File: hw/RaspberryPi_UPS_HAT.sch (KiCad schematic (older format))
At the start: 57 parts, among them J1 ISP, J2 Raspberry_Pi_2_3, J3 BAT, J4 COM, J5 FAN, J6 USB4125-GF-A_REVA, Q1 BC846, Q2 BC846, Q3 AO3401A, Q4 AO3401A, Q5 AO3401A, SW1 BTN, SW2 RST, U1 MIC5219-3.3YM5, U2 ATtiny841-SSU, U3 DS18B20, U4 MT3608, U5 LTC4054ES5-4.2

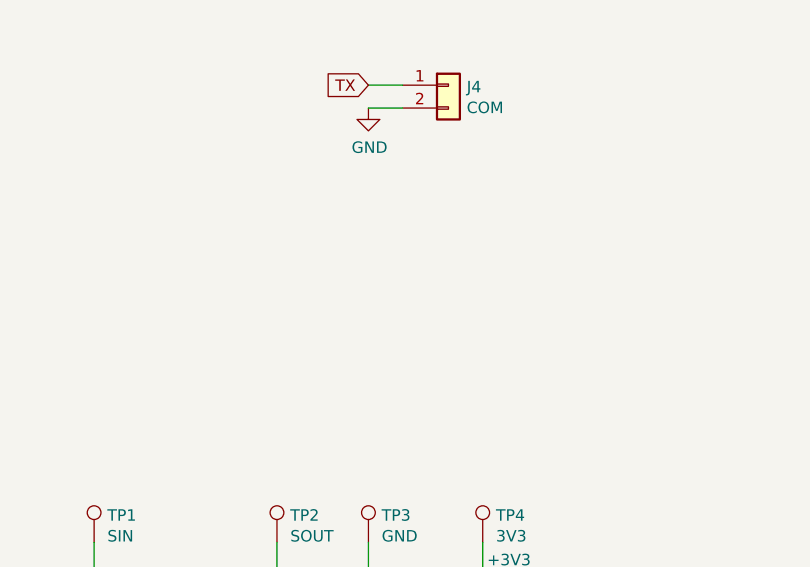
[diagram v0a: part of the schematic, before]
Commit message: update: make BTN available as optional pin header
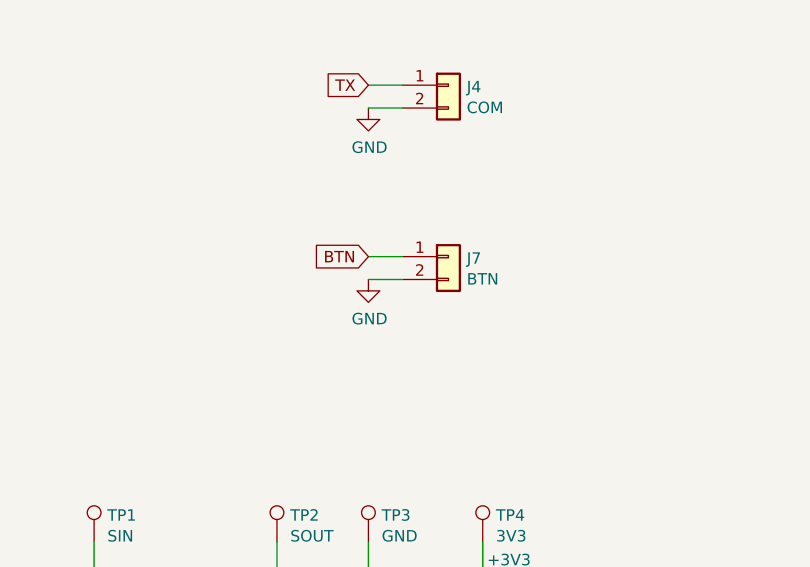
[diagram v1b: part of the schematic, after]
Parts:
- added J7: BTN, Connector_PinHeader_2.54mm:PinHeader_1x02_P2.54mm_Horizontal, symbol Connector_Generic:Conn_01x02
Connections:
- net BTN: now also J7.1 (Pin_1)
- net GND: now also J7.2 (Pin_2)
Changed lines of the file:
@@
 Wire Wire Line
 	9300 10850 9300 11050
+$Comp
+L Connector_Generic:Conn_01x02 J7
+U 1 1 61B850AD
+P 15250 8250
+F 0 "J7" H 15330 8242 50  0000 L CNN
+F 1 "BTN" H 15330 8151 50  0000 L CNN
+F 2 "Connector_PinHeader_2.54mm:PinHeader_1x02_P2.54mm_Horizontal" H 15250 8250 50  0001 C CNN
+F 3 "~" H 15250 8250 50  0001 C CNN
+	1    15250 8250
+	1    0    0    -1
+$EndComp
+$Comp
+L power:GND #PWR035
+U 1 1 61B85901
+P 14900 8350
+F 0 "#PWR035" H 14900 8100 50  0001 C CNN
+F 1 "GND" H 14905 8177 50  0000 C CNN
+F 2 "" H 14900 8350 50  0001 C CNN
+F 3 "" H 14900 8350 50  0001 C CNN
+	1    14900 8350
+	1    0    0    -1
+$EndComp
+Wire Wire Line
+	15050 8250 14900 8250
+Wire Wire Line
+	15050 8350 14900 8350
+Text GLabel 14900 8250 0    50   Input ~ 0
+BTN
 $EndSCHEMATC
